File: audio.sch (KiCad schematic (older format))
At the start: 1 part, among them J6 Audio-Jack-5

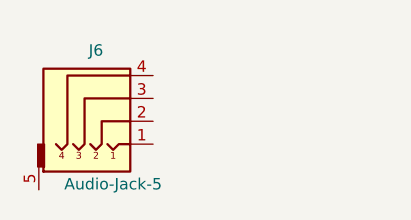
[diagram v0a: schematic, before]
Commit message: schematics: correct audio jack and return of footprint association for fpga chip
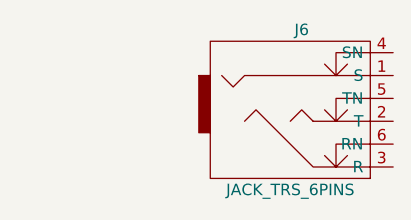
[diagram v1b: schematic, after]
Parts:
- removed J6: Audio-Jack-5, audio-jack:CUI_SJ-43516-SMT, symbol Audio-Jack-5
- added J6: JACK_TRS_6PINS, audio-jack:CUI_SJ-43516-SMT, symbol JACK_TRS_6PINS
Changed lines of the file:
@@
 $EndDescr
 $Comp
-L Audio-Jack-5 J6
-U 1 1 5A133C61
-P 2850 3150
-F 0 "J6" H 2800 3360 50  0000 C CNN
-F 1 "Audio-Jack-5" H 2875 2775 50  0000 C CNN
-F 2 "audio-jack:CUI_SJ-43516-SMT" H 3100 3250 50  0001 C CNN
-F 3 "" H 3100 3250 50  0001 C CNN
-	1    2850 3150
+L JACK_TRS_6PINS J6
+U 1 1 5A13FDB0
+P 3700 3250
+F 0 "J6" H 3700 3650 50  0000 C CNN
+F 1 "JACK_TRS_6PINS" H 3650 2950 50  0000 C CNN
+F 2 "audio-jack:CUI_SJ-43516-SMT" H 3800 3100 60  0001 C CNN
+F 3 "" H 3800 3100 60  0000 C CNN
+	1    3700 3250
 	1    0    0    -1
 $EndComp
